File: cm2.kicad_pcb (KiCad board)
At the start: 2 copper layers, 597 parts, among them J1 Conn_02x06_Counter_Clockwise, J2 Conn_02x06_Counter_Clockwise, J3 Raspberry_Pi_2_3, J4 Screw_Terminal_01x02, J5 Screw_Terminal_01x02, J6 Conn_02x06_Counter_Clockwise, J7 Conn_02x06_Counter_Clockwise, U1 HT1632C-52LQFP, U2 HT1632C-52LQFP

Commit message: checkpoint
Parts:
- removed REF** (x6): MountingHole_3.2mm_M3, MountingHole:MountingHole_3.2mm_M3
- added C10: 10uF, Capacitor_SMD:C_1206_3216Metric_Pad1.33x1.80mm_HandSolder, F.Cu at (-23.2, 233.4)
- added C7: 10uF, Capacitor_SMD:C_1206_3216Metric_Pad1.33x1.80mm_HandSolder, F.Cu at (-61.1, 66.8)
- added C8: 10uF, Capacitor_SMD:C_1206_3216Metric_Pad1.33x1.80mm_HandSolder, F.Cu at (-59.3, 165.5)
- added C9: 10uF, Capacitor_SMD:C_1206_3216Metric_Pad1.33x1.80mm_HandSolder, F.Cu at (-23.4, 0.00)
- added H1: Frame MountingHole, MountingHole:MountingHole_3.2mm_M3, F.Cu at (506.1, 5.97)
- added H10: RPi MountingHole, MountingHole:MountingHole_2.5mm, F.Cu at (-31.5, 57.9)
- added H2: RPi MountingHole, MountingHole:MountingHole_2.5mm, F.Cu at (-55.1, 116.6)
- added H3: Frame MountingHole, MountingHole:MountingHole_3.2mm_M3, F.Cu at (502.9, 119.8)
- added H4: Frame MountingHole, MountingHole:MountingHole_3.2mm_M3, F.Cu at (-9.65, -5.08)
- added H5: Frame MountingHole, MountingHole:MountingHole_3.2mm_M3, F.Cu at (503.2, 230.1)
- added H6: Frame MountingHole, MountingHole:MountingHole_3.2mm_M3, F.Cu at (-8.51, 118.6)
- added H7: Frame MountingHole, MountingHole:MountingHole_3.2mm_M3, F.Cu at (-9.91, 229.0)
- added H8: RPi MountingHole, MountingHole:MountingHole_2.5mm, F.Cu at (-31.0, 116.8)
- added H9: RPi MountingHole, MountingHole:MountingHole_2.5mm, F.Cu at (-54.7, 58.0)
- J1: value Conn_02x06_Counter_Clockwise -> top left
- J2: value Conn_02x06_Counter_Clockwise -> bottom left
- moved J2 549.3 mm to (-29.7, 237.4)
- moved J1 547.6 mm to (-29.3, -3.43)
- moved J6 538.2 mm to (509.1, -3.43)
- moved J7 537.7 mm to (509.0, 242.6)
- moved R64 321.4 mm to (499.1, 191.8)
- moved R63 311.4 mm to (483.2, 191.8)
- moved R62 301.4 mm to (467.4, 191.8)
- moved R61 291.5 mm to (451.5, 191.8)
- moved R60 281.5 mm to (435.6, 191.5)
- moved R59 271.6 mm to (419.7, 191.5)
- moved R58 264.5 mm to (403.7, 175.4)
- moved R57 254.7 mm to (387.9, 175.4)
- moved R56 244.9 mm to (372.0, 175.4)
- moved R55 235.1 mm to (356.1, 175.4)
- moved R54 225.3 mm to (340.2, 175.4)
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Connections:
- J1 pad 1: (no net) -> +5V
- J1 pad 10: (no net) -> GND
- J1 pad 11: (no net) -> GND
- J1 pad 12: (no net) -> GND
- J1 pad 2: (no net) -> +5V
- J1 pad 3: (no net) -> +5V
- J1 pad 4: (no net) -> +5V
- J1 pad 5: (no net) -> /DATA
- J1 pad 6: (no net) -> /~CE0
- J1 pad 7: (no net) -> /~WR
- J1 pad 8: (no net) -> /~CE1
- J1 pad 9: (no net) -> GND
- J2 pad 1: (no net) -> +5V
- J2 pad 10: (no net) -> GND
- J2 pad 11: (no net) -> GND
- J2 pad 12: (no net) -> GND
- J2 pad 2: (no net) -> +5V
- J2 pad 3: (no net) -> +5V
- J2 pad 4: (no net) -> +5V
- J2 pad 5: (no net) -> /DATA
- J2 pad 6: (no net) -> /~CE2
- J2 pad 7: (no net) -> /~WR
- J2 pad 8: (no net) -> /~CE3
- J2 pad 9: (no net) -> GND
- J3 pad 19: (no net) -> /DATA
- J3 pad 20: (no net) -> GND
- J3 pad 23: (no net) -> /~WR
- J3 pad 24: (no net) -> /~CE0
- J3 pad 25: (no net) -> GND
- J3 pad 26: (no net) -> /~CE1
- J3 pad 27: (no net) -> /~CE2
- J3 pad 28: (no net) -> /~CE3
- J3 pad 30: (no net) -> GND
- J3 pad 34: (no net) -> GND
- J3 pad 39: (no net) -> GND
- J6 pad 1: (no net) -> +5V
- J6 pad 11: (no net) -> +5V
- J6 pad 12: (no net) -> +5V
- J6 pad 2: (no net) -> +5V
- J6 pad 5: (no net) -> GND
- J6 pad 6: (no net) -> GND
- J6 pad 7: (no net) -> GND
- J6 pad 8: (no net) -> GND
- J7 pad 1: (no net) -> +5V
- J7 pad 11: (no net) -> +5V
- J7 pad 12: (no net) -> +5V
- J7 pad 2: (no net) -> +5V
- J7 pad 5: (no net) -> GND
- J7 pad 6: (no net) -> GND
- J7 pad 7: (no net) -> GND
- J7 pad 8: (no net) -> GND
- U1 pad 16: (no net) -> /DATA
- U1 pad 17: (no net) -> /~WR
- U2 pad 16: (no net) -> /DATA
- U2 pad 17: (no net) -> /~WR
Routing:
- net /row63: track 0.00 -> 553.6 mm
- net /row62: track 0.00 -> 545.5 mm
- net /row61: track 0.00 -> 528.7 mm
- net /row60: track 0.00 -> 511.8 mm
- net /row59: track 0.00 -> 494.9 mm
- net /row58: track 0.00 -> 477.8 mm
- net /row57: track 0.00 -> 431.6 mm
- net /row56: track 0.00 -> 415.2 mm
- net /row55: track 0.00 -> 400.7 mm
- net /row54: track 0.00 -> 384.2 mm
- net /row53: track 0.00 -> 368.8 mm
- net /row52: track 0.00 -> 353.9 mm
- net /row51: track 0.00 -> 328.0 mm
- net /row50: track 0.00 -> 312.0 mm
- net /row49: track 0.00 -> 294.4 mm
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- added copper zone on B.Cu, net (none)
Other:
- board outline added: 615 x 260 mm
- board text added: "Board Corner Radius = 3mm All holes are M2.5"
- board text added: "Board dimensions are on Cmts (Comments) layer. Deselect it in Layers Manager to make them invisible. GPIO connector nets are not connected, these will get updated as per your schematic/netlist."

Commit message: continue wiring -- 3hr
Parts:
- moved C4 73.8 mm to (-36.8, 148.8)
- moved R44 15.9 mm to (181.1, 159.8)
- moved J1 12.7 mm to (-42.0, -3.43)
- moved J4 10.9 mm to (-56.9, 4.83)
- moved C1 7.63 mm to (-49.3, -2.41), turned to 180 degrees
- moved R64 6.66 mm to (494.7, 196.7)
- turned C3 to 180 degrees
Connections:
- J1 pad 3: +5V -> /~CS0
- J1 pad 5: /DATA -> /~WR
- J1 pad 6: /~CE0 -> +5V
- J1 pad 7: /~WR -> /DATA
- J1 pad 8: /~CE1 -> GND
- J1 pad 9: GND -> /~CS1
- J2 pad 3: +5V -> /~CS2
- J2 pad 5: /DATA -> /~WR
- J2 pad 6: /~CE2 -> +5V
- J2 pad 7: /~WR -> /DATA
- J2 pad 8: /~CE3 -> GND
- J2 pad 9: GND -> /~CS3
- J3 pad 24: /~CE0 -> /~CS0
- J3 pad 26: /~CE1 -> /~CS1
- J3 pad 27: /~CE2 -> /~CS2
- J3 pad 28: /~CE3 -> /~CS3
- U1 pad 19: (no net) -> /~CS0
- U2 pad 19: (no net) -> /~CS1
- U2 pad 21: (no net) -> +5V
- U2 pad 38: (no net) -> +5V
- U2 pad 7: (no net) -> +5V
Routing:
- net /col15: track 291.6 -> 888.7 mm
- net /col14: track 254.6 -> 850.5 mm
- net /col13: track 219.3 -> 811.7 mm
- net /col12: track 182.9 -> 772.8 mm
- net /col08: track 66.5 -> 649.9 mm
- net /col09: track 91.9 -> 660.9 mm
- net /col10: track 127.6 -> 690.7 mm
- net /col11: track 196.0 -> 735.2 mm
- net /~CS1: track 0.00 -> 165.5 mm, vias 0 -> 1
- net /DATA: track 0.00 -> 163.2 mm, vias 0 -> 2
- net /~WR: track 0.00 -> 162.9 mm, vias 0 -> 2
- net /~CS0: track 0.00 -> 98.6 mm, vias 0 -> 1
- net /row63: track 553.6 -> 572.6 mm
- net /row51: track 328.0 -> 345.9 mm
- net /row40: track 149.5 -> 167.1 mm
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- removed copper zone on B.Cu, net (none)

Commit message: wiring, mpunting holes, 3h
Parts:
- added H11: Frame MountingHole, MountingHole:MountingHole_3.2mm_M3, F.Cu at (247.5, 230.2)
- added H12: Frame MountingHole, MountingHole:MountingHole_3.2mm_M3, F.Cu at (247.5, -5.00)
- added H13: Frame MountingHole, MountingHole:MountingHole_3.2mm_M3, F.Cu at (247.5, 119.1)
- added H14: Frame MountingHole, MountingHole:MountingHole_3.2mm_M3, F.Cu at (120.5, -5.00)
- added H15: Frame MountingHole, MountingHole:MountingHole_3.2mm_M3, F.Cu at (120.5, 119.1)
- added H16: Frame MountingHole, MountingHole:MountingHole_3.2mm_M3, F.Cu at (120.5, 230.2)
- added H17: Frame MountingHole, MountingHole:MountingHole_3.2mm_M3, F.Cu at (358.4, 119.1)
- added H18: Frame MountingHole, MountingHole:MountingHole_3.2mm_M3, F.Cu at (358.4, -5.00)
- added H19: Frame MountingHole, MountingHole:MountingHole_3.2mm_M3, F.Cu at (358.4, 230.2)
- moved H1 12.0 mm to (501.1, -5.00)
- moved H5 2.05 mm to (501.1, 230.2)
- moved H3 1.96 mm to (501.1, 119.1)
- moved H7 1.52 mm to (-9.00, 230.2)
- moved H6 0.66 mm to (-9.00, 119.1)
- moved H4 0.66 mm to (-9.00, -5.00)
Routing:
- net /col00: track 661.3 -> 664.6 mm
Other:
- board size 615 x 260 mm -> 615 x 254 mm
- board text added: "LED pitch is 0.625" = .625 * 25.4 = 15.875mm Board dimensions (height) is 16 * led pitch = 264mm top = -10mm bottom = 254 left = right = holes for vertical struts are centered 9 mm to left and right of array so at y = -9mm and (32*pitch) + 9 = 517mm horizontal strut is midpoint of the array, or 8.5 * pitch or 134.94 mm Borders of 10mm on top and 5.875mm on bottom so boards can mate top to bottom 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"

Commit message: checkpoint
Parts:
- moved C2 17.1 mm to (-51.8, 225.3)
- moved C7 14.1 mm to (-49.7, 75.1), turned to 90 degrees
- moved J2 13.9 mm to (-42.0, 230.9)
- moved C10 12.4 mm to (-33.8, 226.9)
- moved J7 11.7 mm to (510.0, 230.9)
- moved C8 11.1 mm to (-50.2, 171.8), turned to 270 degrees
- moved C9 4.83 mm to (-25.5, -4.32), turned to 90 degrees
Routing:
- net /~CS3: track 0.00 -> 162.5 mm, vias 0 -> 1
- net /~CS2: track 0.00 -> 142.8 mm
- net /DATA: track 163.2 -> 261.9 mm, vias 2 -> 3
- net /~WR: track 162.9 -> 259.5 mm, vias 2 -> 3
- net +5V: track 96.9 -> 116.0 mm, vias 4 -> 12
- net /~CS1: track 165.5 -> 184.6 mm, vias 1 -> 3
- net /~CS0: track 98.6 -> 114.4 mm, vias 1 -> 2
- net GND: track 50.6 -> 57.8 mm, vias 7 -> 9
- net (no net): vias 1 -> 0

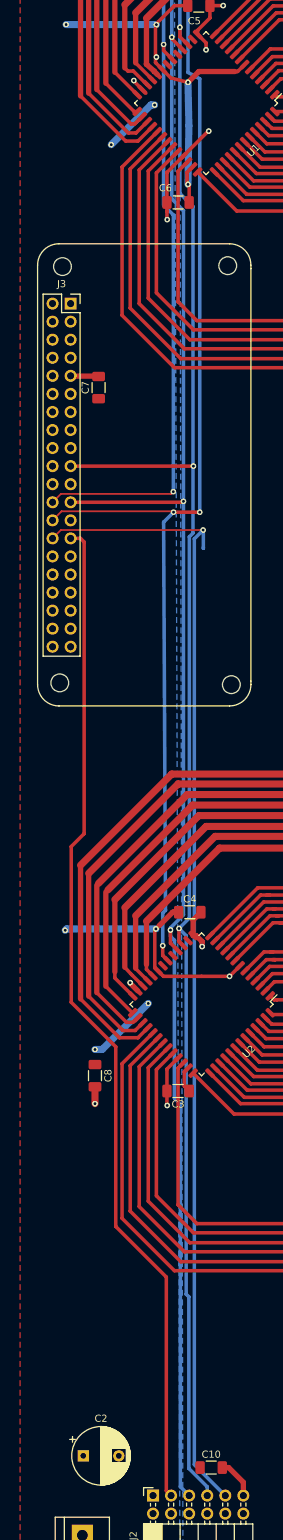
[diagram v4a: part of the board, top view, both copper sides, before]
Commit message: get rpi dimensions exact, rerout chip selects, 2 hrs
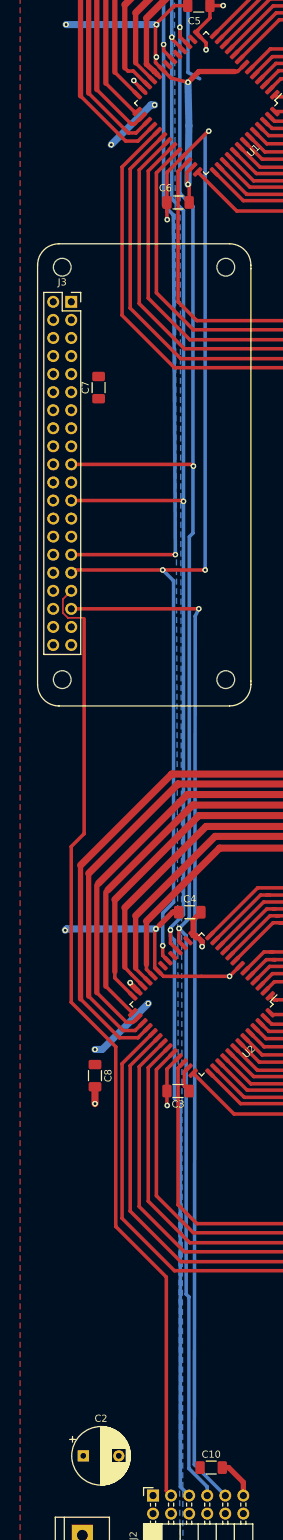
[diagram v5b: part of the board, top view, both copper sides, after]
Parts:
- moved H8 1.06 mm to (-31.8, 116.1)
- moved H2 0.57 mm to (-54.8, 116.1)
- moved H10 0.35 mm to (-31.8, 58.1)
- moved J3 0.26 mm to (-53.5, 63.0)
- moved H9 0.09 mm to (-54.7, 58.1)
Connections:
- J3 pad 24: /~CS0 -> (no net)
- J3 pad 26: /~CS1 -> (no net)
- J3 pad 27: /~CS2 -> (no net)
- J3 pad 28: /~CS3 -> (no net)
- J3 pad 29: (no net) -> /~CS0
- J3 pad 31: (no net) -> /~CS1
- J3 pad 33: (no net) -> /~CS2
- J3 pad 35: (no net) -> /~CS3
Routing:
- net /~CS3: track 162.5 -> 144.8 mm
- net /~CS1: track 184.6 -> 176.8 mm
- net /~CS2: track 142.8 -> 136.8 mm
- net /~CS0: track 114.4 -> 120.3 mm
- net GND: track 57.8 -> 53.8 mm

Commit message: Final board check, tape out, and submit. 3hrs
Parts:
- removed J6: Conn_02x06_Counter_Clockwise, Connector_PinHeader_2.54mm:PinHeader_2x06_P2.54mm_Horizontal
- removed J7: Conn_02x06_Counter_Clockwise, Connector_PinSocket_2.54mm:PinSocket_2x06_P2.54mm_Horizontal
- added ?: , , F.Cu at (-30.0, 215.4)
- added C11: 100uF, Capacitor_SMD:CP_Elec_6.3x7.7, F.Cu at (-55.6, 6.86)
- added C12: 100uF, Capacitor_SMD:CP_Elec_6.3x7.7, F.Cu at (-49.5, 215.6)
- C1, C2: footprint Capacitor_THT:CP_Radial_D8.0mm_P5.00mm -> Capacitor_THT:CP_Radial_D6.3mm_P2.50mm
- moved J4 27.7 mm to (-57.7, 32.5)
- moved C7 19.7 mm to (-48.8, 94.7), turned to 180 degrees
- moved C10 9.79 mm to (-25.4, 231.9), turned to 90 degrees
- moved C1 5.34 mm to (-54.6, -2.29)
- moved J5 3.38 mm to (-53.8, 233.7)
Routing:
- net GND: track 53.8 -> 70.0 mm
- net /~CS1: track 176.8 -> 185.4 mm
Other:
- board size 615 x 254 mm -> 571.1 x 254 mm
- board text added: "+5V"
- board text added: "CM2 led array J Foote 2021 rotormind.com"
- board text added: "DATA"
- board text added: "GND"
- board text added: "PIN 1 ▲"
- board text added: "~CS0"
- board text added: "~CS1"
- board text added: "~CS2"
- board text added: "~CS3"
- board text added: "~WR"
- board text added: "▲"

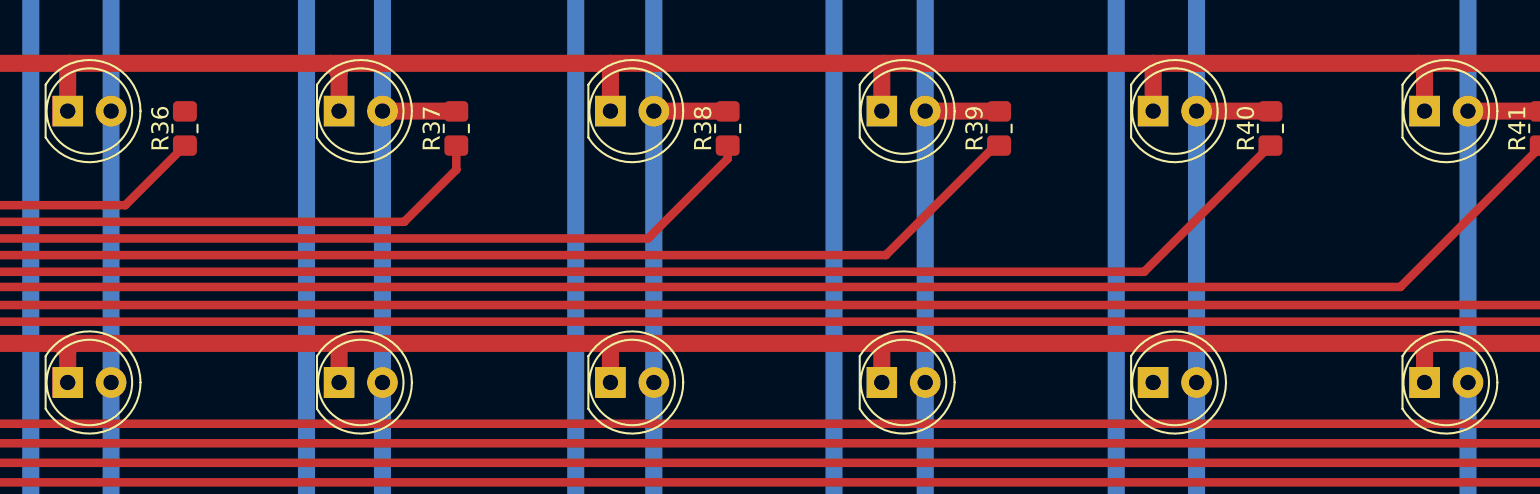
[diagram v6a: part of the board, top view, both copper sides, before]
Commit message: different libs for servertest
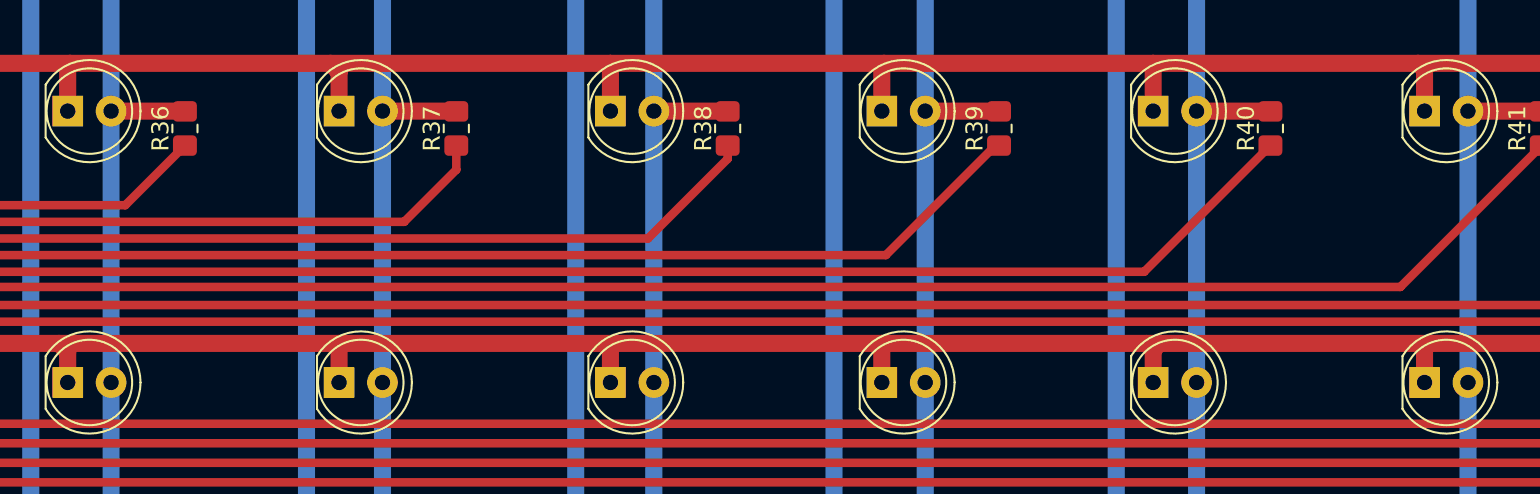
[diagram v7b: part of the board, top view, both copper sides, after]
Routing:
- net Net-(D03A2-Pad2): track 111.1 -> 115.4 mm
- net /col10: track 690.7 -> 693.2 mm
